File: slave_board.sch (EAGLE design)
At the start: 149 parts, among them IC1 NCP1117ST50T3G, IC2 NCP1117ST50T3G, IC3 ATMEGA2560-16AU, J17 RJ45, J22 RJ45, J3 1935161, K1 ORWH-SH-112D1F, Q1 PHB45NQ15T, Q2 PHB45NQ15T, Q5 BSS138L, Q7 PHB45NQ15T, Q8 IRFR9024TRPBF, U1 VNQ5E160KTR-E, U3 INA213AIDCKT, U4 VNH7070ASTR, U5 VNH7070ASTR, U6 VNQ5E160KTR-E, U7 INA213AIDCKT, Y1 ABLS-16.000MHZ-B4-T

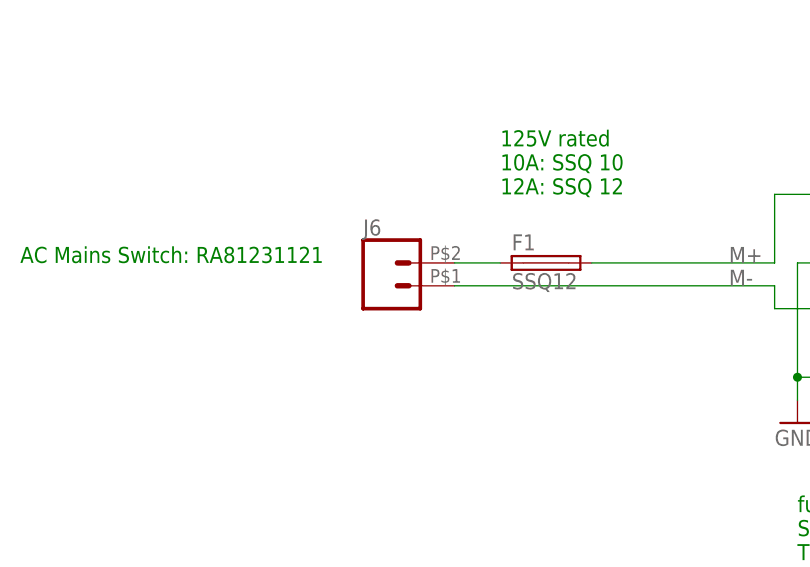
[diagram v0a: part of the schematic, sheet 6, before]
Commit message: mains connector change
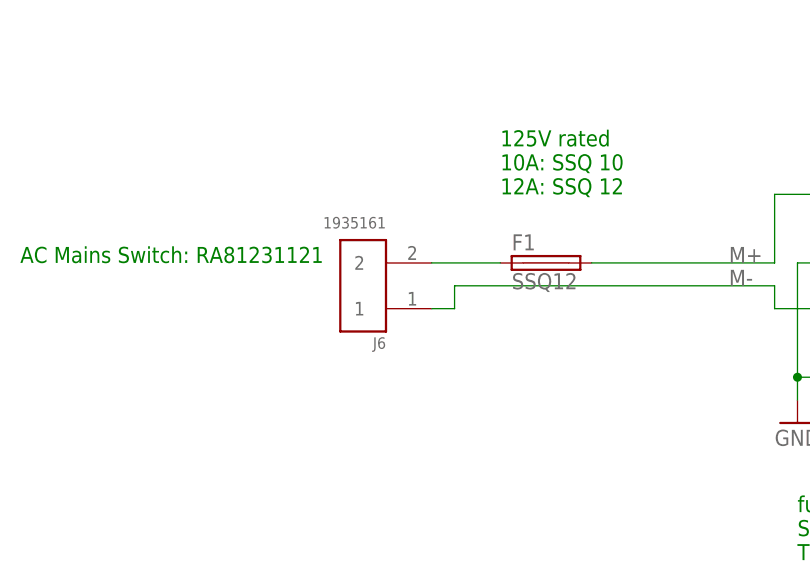
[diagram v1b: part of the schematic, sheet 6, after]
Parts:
- J6: value (none) -> 1935161; device SparkFun-Connectors:CONN_02PTH2 -> 1935161:1935161
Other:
- note added: "OSTVN06A150"
- note removed: "Note: HV devices have wider connector holes for direct soldering of heavy duty wires. Ensure hole diameter and spacing is suitable"
- moved on the sheet: J6
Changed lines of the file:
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@@
 <part name="GND32" library="supply1" library_urn="urn:adsk.eagle:library:371" deviceset="GND" device=""/>
 <part name="U$3" library="SparkFun_Differential_I2C_Breakout_PCA9615_Qwiic" deviceset="SPARKFUN-IC-COMMS_PCA9615" device=""/>
-<part name="J6" library="SparkFun-Connectors" library_urn="urn:adsk.eagle:library:513" deviceset="CONN_02" device="PTH2" package3d_urn="urn:adsk.eagle:package:38043/1"/>
 <part name="GND35" library="supply1" library_urn="urn:adsk.eagle:library:371" deviceset="GND" device=""/>
 <part name="J7" library="SparkFun-Connectors" library_urn="urn:adsk.eagle:library:513" deviceset="CONN_02" device="" package3d_urn="urn:adsk.eagle:package:38039/1"/>
@@
 <part name="GND64" library="supply1" library_urn="urn:adsk.eagle:library:371" deviceset="GND" device=""/>
 <part name="GND72" library="supply1" library_urn="urn:adsk.eagle:library:371" deviceset="GND" device=""/>
+<part name="J6" library="1935161" deviceset="1935161" device=""/>
 </parts>
 <sheets>
@@
 </text>
 <text x="302.26" y="190.5" size="1.778" layer="91">put 47uF capacitor as close as possible to chip</text>
-<text x="137.16" y="248.92" size="1.778" layer="91">Note: HV devices have wider connector holes for direct soldering of heavy duty wires.
-Ensure hole diameter and spacing is suitable</text>
 <text x="320.04" y="175.26" size="1.778" layer="91">OUTPUT</text>
 <text x="373.38" y="208.28" size="1.778" layer="91">/RESET</text>
@@
 <text x="200.66" y="215.9" size="1.778" layer="91">solder over to provide better conduction</text>
 <text x="266.7" y="101.6" size="1.778" layer="91">drive voltage = 10V</text>
+<text x="154.94" y="243.84" size="1.778" layer="91">OSTVN06A150</text>
 </plain>
 <instances>
@@
 <attribute name="VALUE" x="149.86" y="91.44" size="1.778" layer="96"/>
 </instance>
-<instance part="J6" gate="G$1" x="71.12" y="109.22" smashed="yes">
-<attribute name="VALUE" x="68.58" y="104.394" size="1.778" layer="96" font="vector"/>
-<attribute name="NAME" x="68.58" y="114.808" size="1.778" layer="95" font="vector"/>
-</instance>
 <instance part="GND35" gate="1" x="116.84" y="93.98" smashed="yes">
 <attribute name="VALUE" x="114.3" y="91.44" size="1.778" layer="96"/>
@@
 <attribute name="VALUE" x="185.42" y="231.3686" size="1.778" layer="96"/>
 </instance>
+<instance part="J6" gate="G$1" x="68.58" y="109.22" smashed="yes" rot="R180">
+<attribute name="NAME" x="71.12548125" y="103.492659375" size="1.272740625" layer="95" rot="R180"/>
+<attribute name="VALUE" x="71.12808125" y="116.86423125" size="1.274040625" layer="96" rot="R180"/>
+</instance>
 </instances>
 <busses>
@@
 <net name="M-" class="0">
 <segment>
-<pinref part="J6" gate="G$1" pin="1"/>
 <wire x1="78.74" y1="109.22" x2="114.3" y2="109.22" width="0.1524" layer="91"/>
 <wire x1="114.3" y1="109.22" x2="114.3" y2="106.68" width="0.1524" layer="91"/>
@@
 <pinref part="D4" gate="G$1" pin="A"/>
 <pinref part="D5" gate="G$1" pin="C"/>
+<wire x1="78.74" y1="109.22" x2="78.74" y2="106.68" width="0.1524" layer="91"/>
+<pinref part="J6" gate="G$1" pin="1"/>
+<wire x1="78.74" y1="106.68" x2="76.2" y2="106.68" width="0.1524" layer="91"/>
 </segment>
 </net>
 <net name="N$12" class="0">
 <segment>
-<pinref part="J6" gate="G$1" pin="2"/>
-<wire x1="78.74" y1="111.76" x2="83.82" y2="111.76" width="0.1524" layer="91"/>
+<wire x1="76.2" y1="111.76" x2="83.82" y2="111.76" width="0.1524" layer="91"/>
 <pinref part="F1" gate="G$1" pin="1"/>
+<pinref part="J6" gate="G$1" pin="2"/>
 </segment>
 </net>

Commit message: progress on component placement
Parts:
- removed D18: MBR0530, smoothio:MBR0530
- removed J32: (no value), SparkFun-Connectors:CONN_02
- removed RN4: 4.7K, resistor-dil:4R-NCAT16
- removed U$1: EL3H7, smoothio:EL3H7
- added D14: MBR0530, smoothio:MBR0530
- added J11: 1935161, 1935161:1935161
- added Q3: BSS138L, BSS138L:BSS138L
- added R13, R9: 4.7k, SparkFun-Resistors:4.7KOHM-0603-1/10W-1%
- added R15: 10k, SparkFun-Resistors:10KOHM-0603-1/10W-1%
- R11: value 220 -> 10k; device SparkFun-Resistors:220OHM-0603-1/10W-1% -> SparkFun-Resistors:10KOHM-0603-1/10W-1%
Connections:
- removed net N$11: Q7.G, U$1.3
- removed net N$8: R11.2, U$1.2
- new net N$4: Q3.D, Q7.G, R15.1
- net +12V: now also R15.2; no longer U$1.4
- net +5V: now also Q3.G, R11.2, R13.2, R9.2; no longer RN4B.2, RN4C.2
- net COOLANT_EN: now also Q3.S, R11.1; no longer U$1.1
- net GND: now also D14.A; no longer D18.A, R11.1
- net LIQUID1: now also D14.C; no longer D15.C
- net LIQUID2: now also D15.C; no longer D16.C
- net LIQUID3: now also D16.C; no longer D17.C
- net M-: now also J11.2; no longer J32.2
- net POWDER1: now also D17.C; no longer D18.C
- net SCL: now also R9.1; no longer RN4B.1
- net SDA: now also R13.1; no longer RN4C.1
- net V-HEATPUMP: now also J11.1; no longer J32.1
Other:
- note added: "Notes: Damping resistors on SPI for ICSP? 10k resistor array? 12V input connector: 1935161"
- note added: "change 390 ohm to array"
- note added: "may need to change since only rated for 100V (derating)"
- note added: "populate on master and last slave"
- note added: "put 47uF capacitor as close as possible to chip but not too close that cant solder"
- note removed: "Notes: make custom pins for mains 12 or 14 gauge wire Damping resistors on SPI for ICSP? Add another 5V LDO for cup stepper 12V input connector: 1935161"
- note removed: "add on last slave (i think)"
- note removed: "put 47uF capacitor as close as possible to chip"
- moved on the sheet: D15, D16, D17, Q7, R11

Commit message: board adjustments
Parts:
- added C32: 100n, SmartPrj:C-EU0603-RND
- added C33: 4.7uF, SparkFun-Capacitors:4.7UF0603
- added R20: 0, SparkFun-Resistors:0OHM-0603-1/10W-5%
- added R21, R22: 1M, SparkFun-Resistors:1MOHM-0603-1/4W-5%
- added TP1: TEST-POINT3X5, SparkFun-Connectors:TEST-POINT3X5
- added TP10, TP11, TP12, TP13, TP14, TP15, TP16, TP17, TP18, TP19, TP2, TP3, TP4, TP5, TP6, TP7, TP8, TP9: TEST-POINT3, SparkFun-Connectors:TEST-POINT3
- C1: value 47pF -> 100n; device SparkFun-Capacitors:47PF-0603-50V-5% -> SmartPrj:C-EU0603-RND
- C10: value 47pF -> 0.1uF; device SparkFun-Capacitors:47PF-0603-50V-5% -> SparkFun-Capacitors:0.1UF-0603-25V-(+80/-20%)
- C19, C20, C21: value UHE2A470MPD -> UCS2E470MHD1TO; device smoothio:UHE2A470MPD -> smoothio:UCS2E470MHD1TO
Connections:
- new net N$13: C9.2, R20.1, Y1.1
- net +12V: now also TP2.1
- net +5V: now also C32.1, C33.1, TP18.1
- net BLENDER0-: now also D7.C; no longer D7.A
- net BLENDER1-: now also D8.C; no longer D8.A
- net DSCL+: now also TP10.1
- net DSCL-: now also TP11.1
- net DSDA+: now also TP12.1
- net DSDA-: now also TP13.1
- net GND: now also C32.2, C33.2, D7.A, D8.A, J17.7, J17.8, J22.7, J22.8, R21.1, R22.1, TP3.1, TP4.1, TP5.1, TP6.1; no longer C10.1
- net N$10: now also R22.2
- net N$15: now also R21.2
- net PB1: now also TP9.1
- net PB2: now also TP7.1
- net PB3: now also TP8.1
- net SCL: now also TP14.1
- net SDA: now also TP15.1
- net V-12V_PROT: now also TP17.1
- net V-5_LOAD: now also TP19.1
- net V-HVDC: now also TP1.1; no longer D7.C, D8.C
- net V-STEPPER: now also TP16.1
- net V-THERMISTOR: now also C10.1
- net XTAL2: now also R20.2; no longer C9.2, Y1.1
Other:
- note added: "current sense needs to be in series with switch, not parallel"
- note added: "distribute around board"
- note removed: "may need to change since only rated for 100V (derating)"
- moved on the sheet: C10, C3

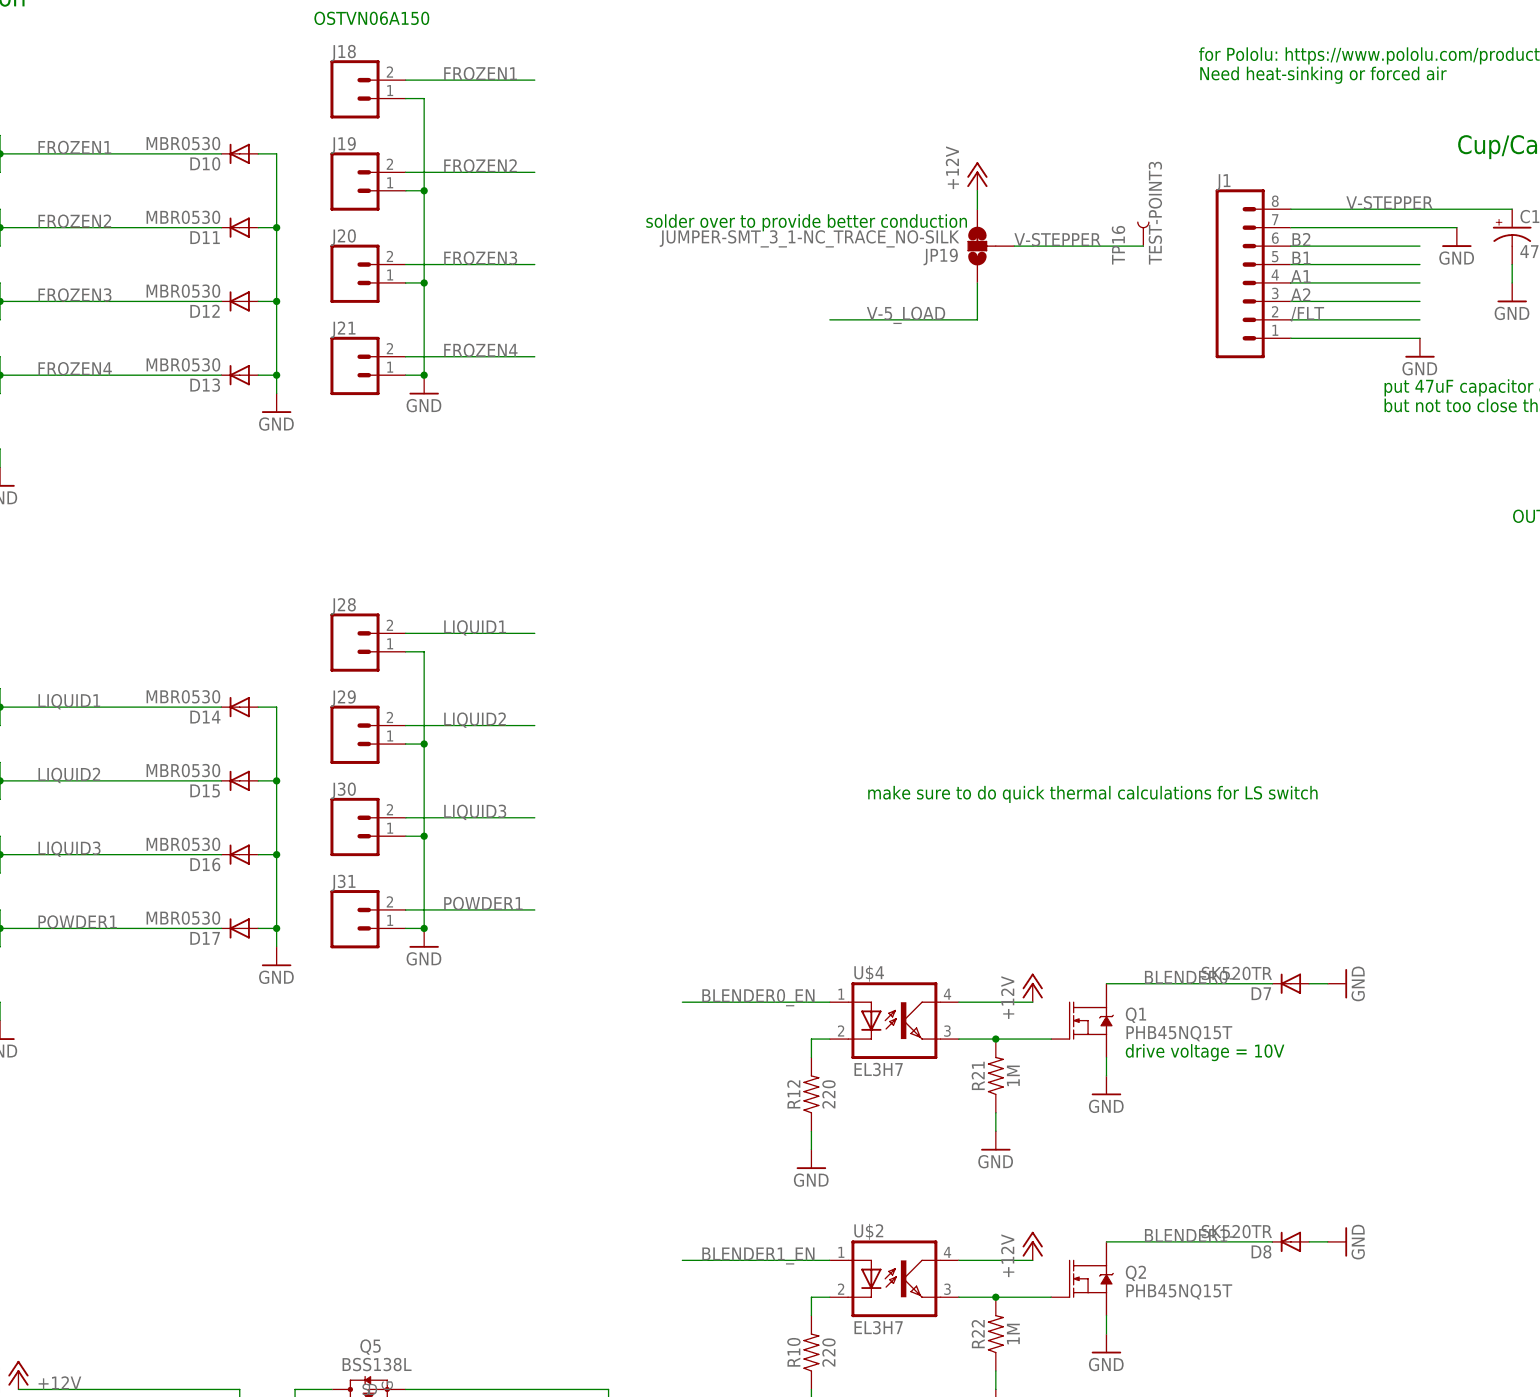
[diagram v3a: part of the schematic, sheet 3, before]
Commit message: fixed current sense
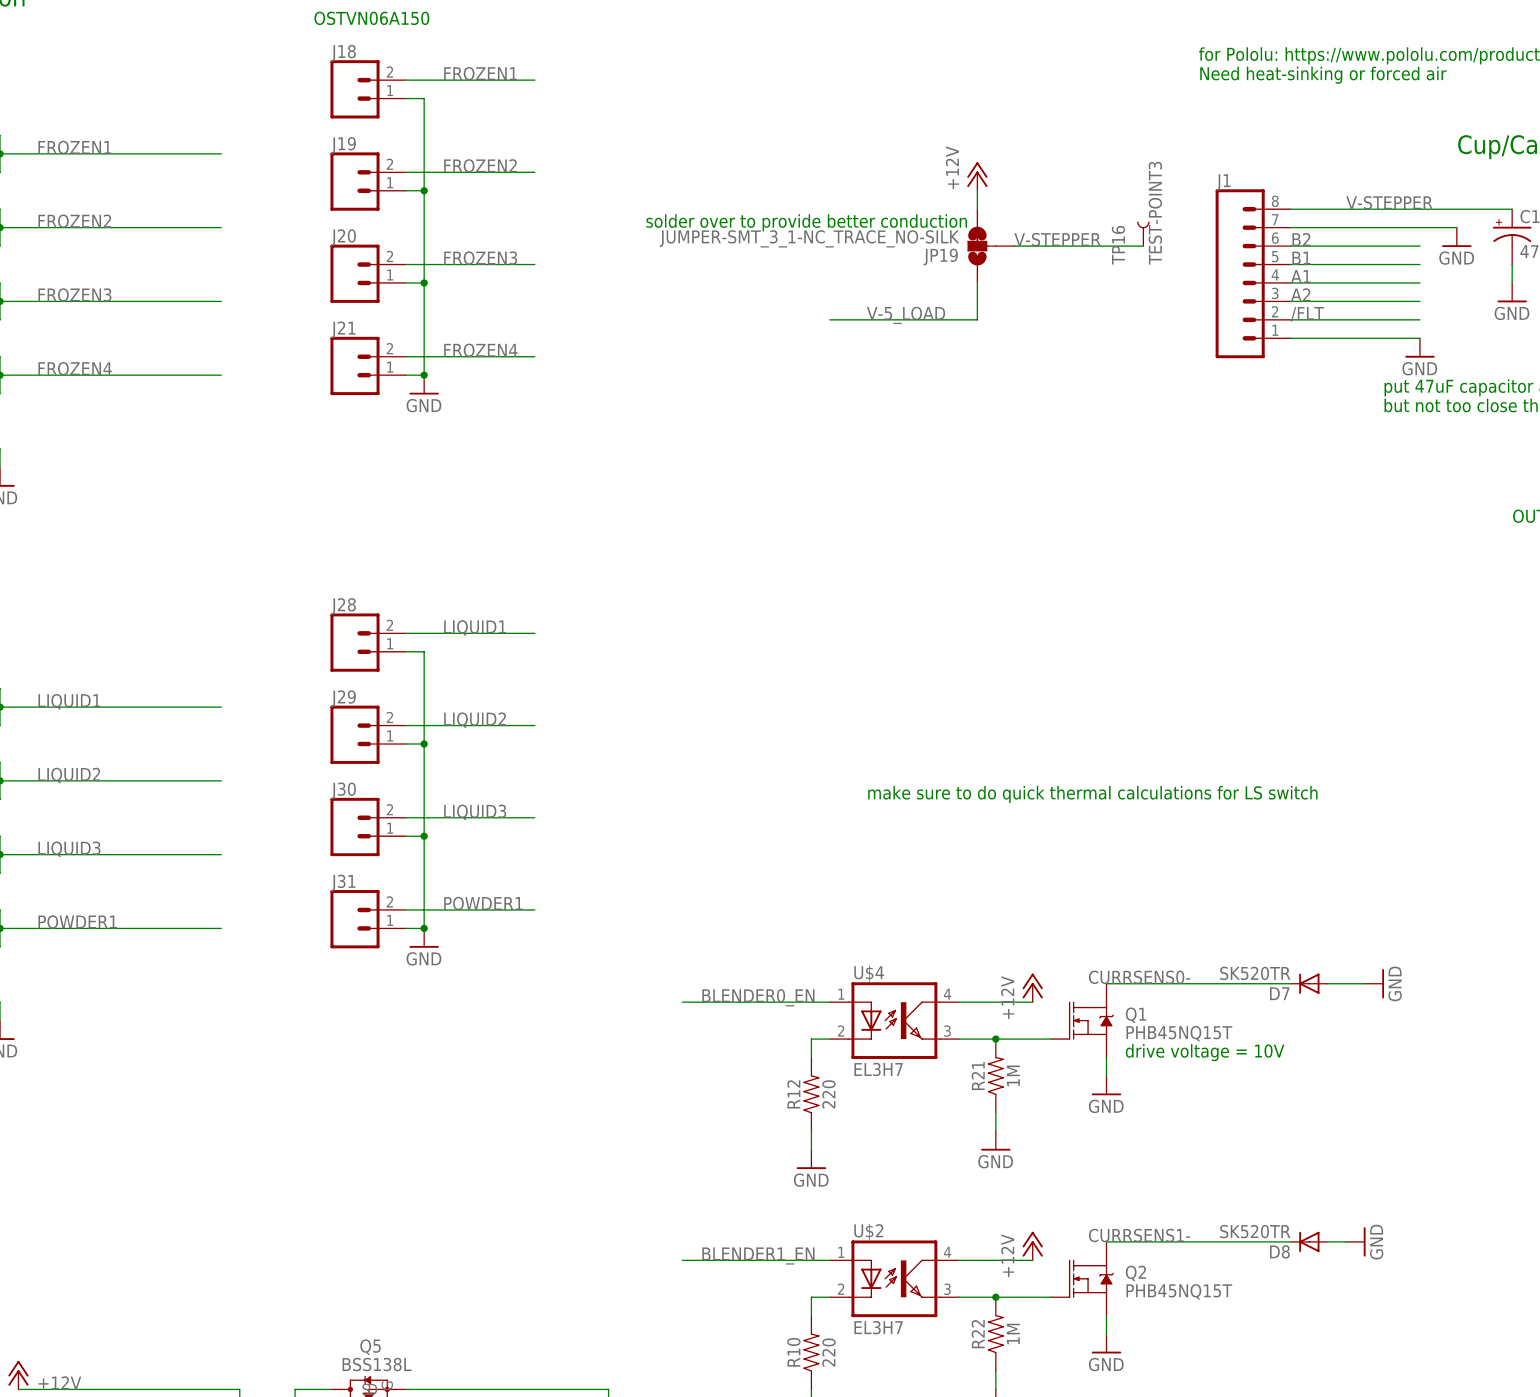
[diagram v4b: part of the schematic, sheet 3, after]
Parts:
- removed D10, D11, D12, D13, D14, D15, D16, D17, D6: MBR0530, smoothio:MBR0530
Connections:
- new net CURRSENS0-: D7.C, Q1.D, R1.1, U3.IN-
- new net CURRSENS1-: D8.C, Q2.D, R14.1, U7.IN-
- net +12V: no longer D6.C
- net BLENDER0-: no longer D7.C, Q1.D
- net BLENDER1-: no longer D8.C, Q2.D
- net COOLANT-: no longer D6.A
- net FROZEN1: no longer D10.C
- net FROZEN2: no longer D11.C
- net FROZEN3: no longer D12.C
- net FROZEN4: no longer D13.C
- net GND: no longer D10.A, D11.A, D12.A, D13.A, D14.A, D15.A, D16.A, D17.A, R1.1, R14.1, U3.IN-, U7.IN-
- net LIQUID1: no longer D14.C
- net LIQUID2: no longer D15.C
- net LIQUID3: no longer D16.C
- net POWDER1: no longer D17.C
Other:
- moved on the sheet: D7, D8
